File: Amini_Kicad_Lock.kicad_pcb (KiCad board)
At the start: 2 copper layers, 24.5 x 19.1 mm, 48 parts, among them J1 Conn_01x02_Pin, J2 Conn_01x04, J3 Conn_01x04_Pin, U1 nRF5340-QKxx, X1 32MHz, X2 32.768kHz

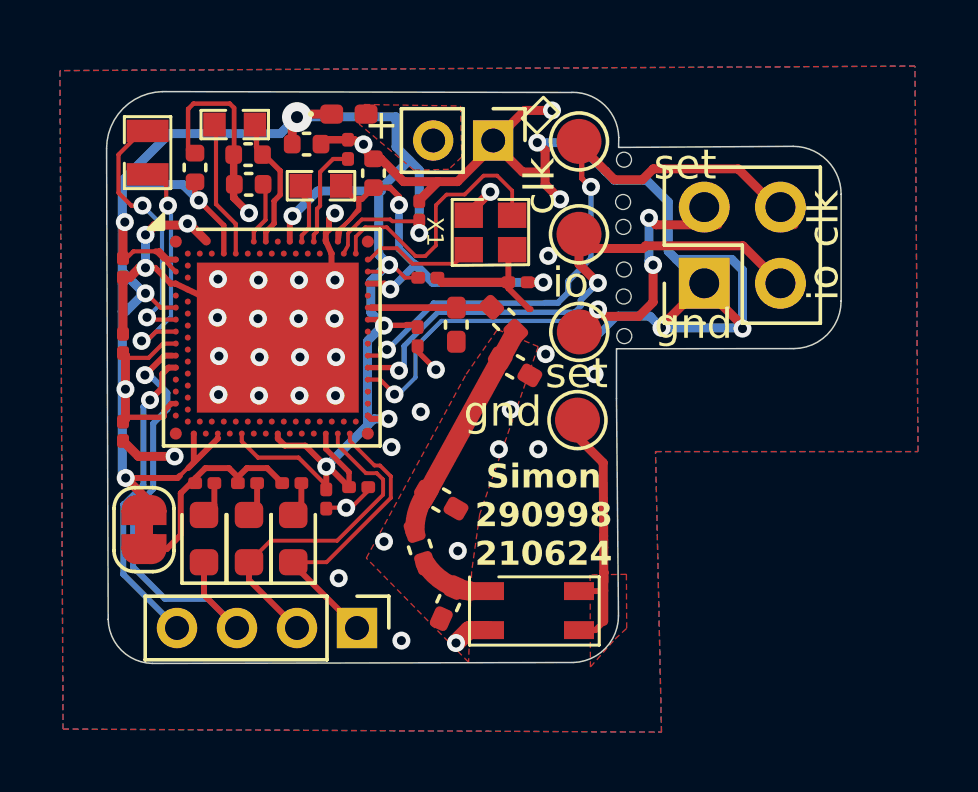
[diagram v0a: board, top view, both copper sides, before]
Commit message: Ryddet opp i schematics
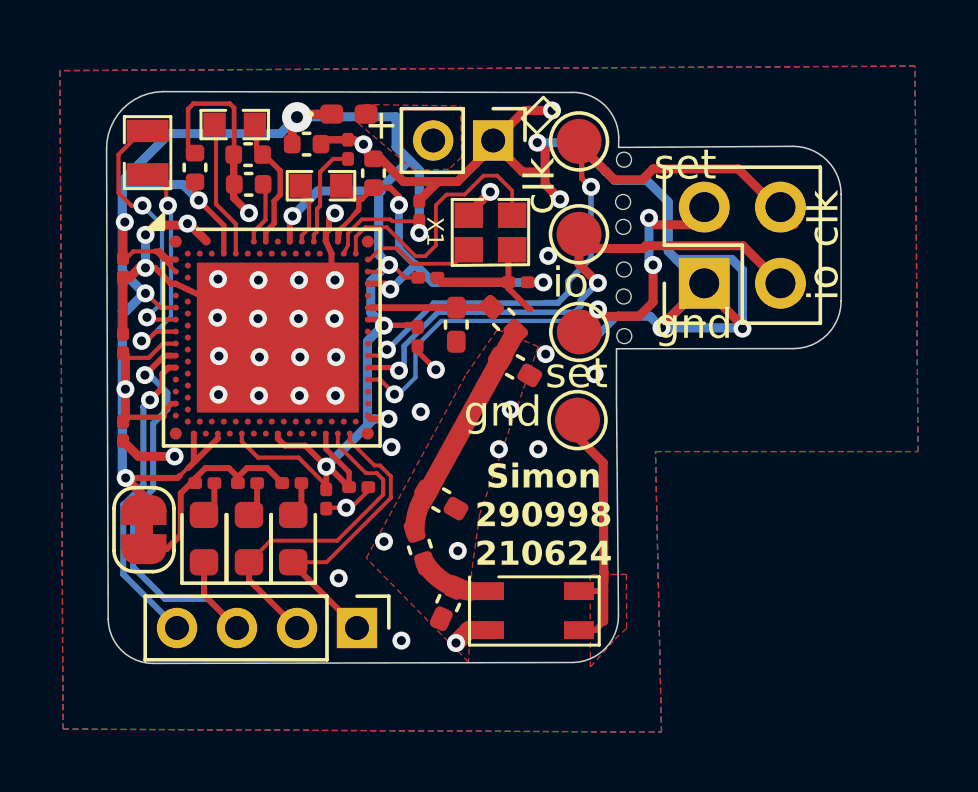
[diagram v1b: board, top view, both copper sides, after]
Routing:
- net GND: track 74.3 -> 75.9 mm
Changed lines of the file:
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@@
+	)
+	(segment
+		(start 190.2 61.525)
+		(end 190.3225 61.4025)
+		(width 0.2)
+		(layer "B.Cu")
+		(net 1)
 	)
 	(segment
@@
 	)
 	(segment
-		(start 190.2 61.525)
-		(end 190.54 61.185)
-		(width 0.3)
-		(layer "B.Cu")
-		(net 1)
-	)
-	(segment
 		(start 188.751653 61.134)
 		(end 188.739653 61.146)
@@
 		(end 188.06 61.79)
 		(width 0.25)
+		(layer "B.Cu")
+		(net 1)
+	)
+	(segment
+		(start 190.3225 61.4025)
+		(end 190.3225 61.3425)
+		(width 0.2)
 		(layer "B.Cu")
 		(net 1)
@@
 		(width 0.3)
 		(layer "B.Cu")
+		(net 1)
+	)
+	(segment
+		(start 190.3225 61.3425)
+		(end 191.625 60.04)
+		(width 0.3)
+		(layer "B.Cu")
